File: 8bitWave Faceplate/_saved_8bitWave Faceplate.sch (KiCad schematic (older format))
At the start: 44 parts, among them IC1 0.96_I2C_OLED, J1 I2C_VOL, J3 EXTENSION, M1 Mounting, M2 Mounting, M3 Mounting, M4 Mounting, U1 74HC595_ALT

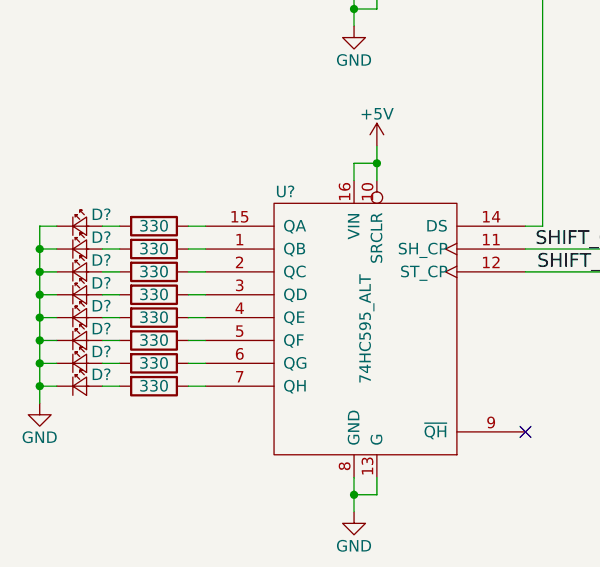
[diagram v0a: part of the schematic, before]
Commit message: Faceplate tracks routed
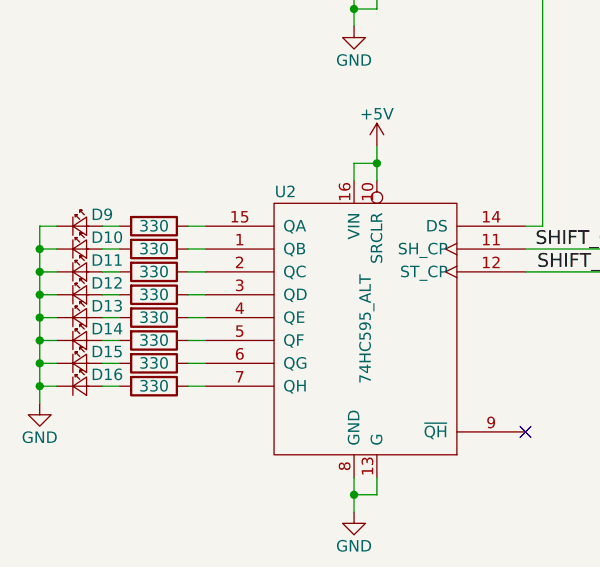
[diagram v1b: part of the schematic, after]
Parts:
- gave numbers to parts that had none: 17
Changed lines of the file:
@@
 Connection ~ 2750 3825
 $Comp
-L GND #PWR?
+L GND #PWR013
 U 1 1 5E3F8B26
 P 4125 7100
-F 0 "#PWR?" H 4125 6850 50  0001 C CNN
+F 0 "#PWR013" H 4125 6850 50  0001 C CNN
 F 1 "GND" H 4125 6950 50  0000 C CNN
 F 2 "" H 4125 7100 50  0001 C CNN
@@
 $EndComp
 $Comp
-L 74HC595_ALT U?
+L 74HC595_ALT U2
 U 1 1 5E3F8B2C
 P 4175 6300
-F 0 "U?" H 4525 6900 50  0000 C CNN
+F 0 "U2" H 4525 6900 50  0000 C CNN
 F 1 "74HC595_ALT" V 4175 6300 50  0000 C CNN
 F 2 "SMD_Packages:SO-16-N" H 4175 6300 50  0001 C CNN
@@
 $EndComp
 $Comp
-L +5V #PWR?
+L +5V #PWR014
 U 1 1 5E3F8B32
 P 4225 5500
-F 0 "#PWR?" H 4225 5350 50  0001 C CNN
+F 0 "#PWR014" H 4225 5350 50  0001 C CNN
 F 1 "+5V" H 4225 5640 50  0000 C CNN
 F 2 "" H 4225 5500 50  0001 C CNN
@@
 NoConn ~ 4875 6750
 $Comp
-L R R?
+L R R9
 U 1 1 5E3F8B4A
 P 3250 5850
-F 0 "R?" V 3330 5850 50  0001 C CNN
+F 0 "R9" V 3330 5850 50  0001 C CNN
 F 1 "330" V 3250 5850 50  0000 C CNN
 F 2 "Resistors_SMD:R_0805_HandSoldering" V 3180 5850 50  0001 C CNN
@@
 	3400 5850 3475 5850
 $Comp
-L LED_Small D?
+L LED_Small D9
 U 1 1 5E3F8B51
 P 2925 5850
-F 0 "D?" H 2975 5900 50  0000 L CNN
+F 0 "D9" H 2975 5900 50  0000 L CNN
 F 1 "RED" H 2750 5750 50  0001 L CNN
 F 2 "LEDs:LED_0805_HandSoldering" V 2925 5850 50  0001 C CNN
@@
 	2825 5850 2750 5850
 $Comp
-L R R?
+L R R10
 U 1 1 5E3F8B59
 P 3250 5950
-F 0 "R?" V 3330 5950 50  0001 C CNN
+F 0 "R10" V 3330 5950 50  0001 C CNN
 F 1 "330" V 3250 5950 50  0000 C CNN
 F 2 "Resistors_SMD:R_0805_HandSoldering" V 3180 5950 50  0001 C CNN
@@
 	3400 5950 3475 5950
 $Comp
-L LED_Small D?
+L LED_Small D10
 U 1 1 5E3F8B60
 P 2925 5950
-F 0 "D?" H 2975 6000 50  0000 L CNN
+F 0 "D10" H 2975 6000 50  0000 L CNN
 F 1 "RED" H 2750 5850 50  0001 L CNN
 F 2 "LEDs:LED_0805_HandSoldering" V 2925 5950 50  0001 C CNN
@@
 	2825 5950 2750 5950
 $Comp
-L R R?
+L R R11
 U 1 1 5E3F8B68
 P 3250 6050
-F 0 "R?" V 3330 6050 50  0001 C CNN
+F 0 "R11" V 3330 6050 50  0001 C CNN
 F 1 "330" V 3250 6050 50  0000 C CNN
 F 2 "Resistors_SMD:R_0805_HandSoldering" V 3180 6050 50  0001 C CNN
@@
 	3400 6050 3475 6050
 $Comp
-L LED_Small D?
+L LED_Small D11
 U 1 1 5E3F8B6F
 P 2925 6050
-F 0 "D?" H 2975 6100 50  0000 L CNN
+F 0 "D11" H 2975 6100 50  0000 L CNN
 F 1 "RED" H 2750 5950 50  0001 L CNN
 F 2 "LEDs:LED_0805_HandSoldering" V 2925 6050 50  0001 C CNN
@@
 	2825 6050 2750 6050
 $Comp
-L R R?
+L R R12
 U 1 1 5E3F8B77
 P 3250 6150
-F 0 "R?" V 3330 6150 50  0001 C CNN
+F 0 "R12" V 3330 6150 50  0001 C CNN
 F 1 "330" V 3250 6150 50  0000 C CNN
 F 2 "Resistors_SMD:R_0805_HandSoldering" V 3180 6150 50  0001 C CNN
@@
 	3400 6150 3475 6150
 $Comp
-L LED_Small D?
+L LED_Small D12
 U 1 1 5E3F8B7E
 P 2925 6150
-F 0 "D?" H 2975 6200 50  0000 L CNN
+F 0 "D12" H 2975 6200 50  0000 L CNN
 F 1 "RED" H 2750 6050 50  0001 L CNN
 F 2 "LEDs:LED_0805_HandSoldering" V 2925 6150 50  0001 C CNN
@@
 	2825 6150 2750 6150
 $Comp
-L R R?
+L R R13
 U 1 1 5E3F8B86
 P 3250 6250
-F 0 "R?" V 3330 6250 50  0001 C CNN
+F 0 "R13" V 3330 6250 50  0001 C CNN
 F 1 "330" V 3250 6250 50  0000 C CNN
 F 2 "Resistors_SMD:R_0805_HandSoldering" V 3180 6250 50  0001 C CNN
@@
 	3400 6250 3475 6250
 $Comp
-L LED_Small D?
+L LED_Small D13
 U 1 1 5E3F8B8D
 P 2925 6250
-F 0 "D?" H 2975 6300 50  0000 L CNN
+F 0 "D13" H 2975 6300 50  0000 L CNN
 F 1 "RED" H 2750 6150 50  0001 L CNN
 F 2 "LEDs:LED_0805_HandSoldering" V 2925 6250 50  0001 C CNN
@@
 	2825 6250 2750 6250
 $Comp
-L R R?
+L R R14
 U 1 1 5E3F8B95
 P 3250 6350
-F 0 "R?" V 3330 6350 50  0001 C CNN
+F 0 "R14" V 3330 6350 50  0001 C CNN
 F 1 "330" V 3250 6350 50  0000 C CNN
 F 2 "Resistors_SMD:R_0805_HandSoldering" V 3180 6350 50  0001 C CNN
@@
 	3400 6350 3475 6350
 $Comp
-L LED_Small D?
+L LED_Small D14
 U 1 1 5E3F8B9C
 P 2925 6350
-F 0 "D?" H 2975 6400 50  0000 L CNN
+F 0 "D14" H 2975 6400 50  0000 L CNN
 F 1 "RED" H 2750 6250 50  0001 L CNN
 F 2 "LEDs:LED_0805_HandSoldering" V 2925 6350 50  0001 C CNN
@@
 	2825 6350 2750 6350
 $Comp
-L R R?
+L R R15
 U 1 1 5E3F8BA4
 P 3250 6450
-F 0 "R?" V 3330 6450 50  0001 C CNN
+F 0 "R15" V 3330 6450 50  0001 C CNN
 F 1 "330" V 3250 6450 50  0000 C CNN
 F 2 "Resistors_SMD:R_0805_HandSoldering" V 3180 6450 50  0001 C CNN
@@
 	3400 6450 3475 6450
 $Comp
-L LED_Small D?
+L LED_Small D15
 U 1 1 5E3F8BAB
 P 2925 6450
-F 0 "D?" H 2975 6500 50  0000 L CNN
+F 0 "D15" H 2975 6500 50  0000 L CNN
 F 1 "RED" H 2750 6350 50  0001 L CNN
 F 2 "LEDs:LED_0805_HandSoldering" V 2925 6450 50  0001 C CNN
@@
 	2825 6450 2750 6450
 $Comp
-L R R?
+L R R16
 U 1 1 5E3F8BB3
 P 3250 6550
-F 0 "R?" V 3330 6550 50  0001 C CNN
+F 0 "R16" V 3330 6550 50  0001 C CNN
 F 1 "330" V 3250 6550 50  0000 C CNN
 F 2 "Resistors_SMD:R_0805_HandSoldering" V 3180 6550 50  0001 C CNN
@@
 	3400 6550 3475 6550
 $Comp
-L LED_Small D?
+L LED_Small D16
 U 1 1 5E3F8BBA
 P 2925 6550
-F 0 "D?" H 2975 6600 50  0000 L CNN
+F 0 "D16" H 2975 6600 50  0000 L CNN
 F 1 "RED" H 2750 6450 50  0001 L CNN
 F 2 "LEDs:LED_0805_HandSoldering" V 2925 6550 50  0001 C CNN
@@
 	2750 5850 2750 6625
 $Comp
-L GND #PWR?
+L GND #PWR015
 U 1 1 5E3F8BC3
 P 2750 6625
-F 0 "#PWR?" H 2750 6375 50  0001 C CNN
+F 0 "#PWR015" H 2750 6375 50  0001 C CNN
 F 1 "GND" H 2750 6475 50  0000 C CNN
 F 2 "" H 2750 6625 50  0001 C CNN
